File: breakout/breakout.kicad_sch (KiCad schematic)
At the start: 9 parts, among them J1 Glasgow, J2 ScrewTerminals, J3 SignalsMale, J4 SignalsFemale, J5 SignalsMale, J6 SignalsFemale, J7 TestPoints

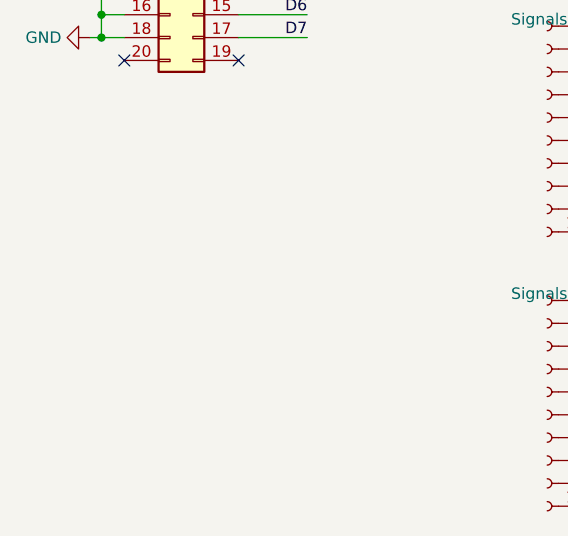
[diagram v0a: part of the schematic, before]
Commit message: [wip] add connector for generic fx2 logic analyzers
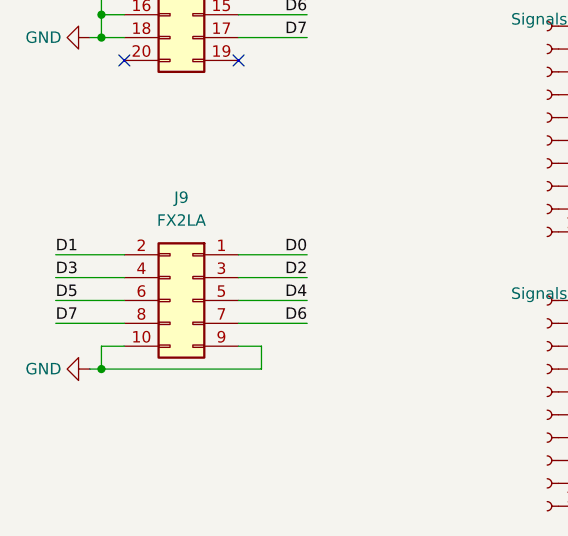
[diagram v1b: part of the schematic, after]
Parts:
- added J9: FX2LA, Connector_PinSocket_2.54mm:PinSocket_2x05_P2.54mm_Vertical, symbol Connector_Generic:Conn_02x05_Odd_Even
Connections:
- net D0: now also J9.1 (Pin_1)
- net D1: now also J9.2 (Pin_2)
- net D2: now also J9.3 (Pin_3)
- net D3: now also J9.4 (Pin_4)
- net D4: now also J9.5 (Pin_5)
- net D5: now also J9.6 (Pin_6)
- net D6: now also J9.7 (Pin_7)
- net D7: now also J9.8 (Pin_8)
- net GND: now also J9.10 (Pin_10), J9.9 (Pin_9)

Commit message: finished
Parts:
- J2: footprint TerminalBlock_Phoenix:TerminalBlock_Phoenix_MPT-0,5-12-2.54_1x12_P2.54mm_Horizontal -> Glasgow:TerminalBlock_not_WAGO_233-512_2x12_P2.54mm
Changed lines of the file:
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@@
 			)
 		)
-		(property "Footprint" "TerminalBlock_Phoenix:TerminalBlock_Phoenix_MPT-0,5-12-2.54_1x12_P2.54mm_Horizontal"
+		(property "Footprint" "Glasgow:TerminalBlock_not_WAGO_233-512_2x12_P2.54mm"
 			(at 171.45 81.28 0)
 			(effects

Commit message: wip? rev2
- rounded corners
- more LA space (todo confirm spacing re: glasgow center)
- vio/vsense connection switch
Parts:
- added SW1: SW_SPDT, Button_Switch_THT:SW_Slide_SPDT_Straight_CK_OS102011MS2Q, symbol Switch:SW_SPDT
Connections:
- net VBUS: now also SW1.2 (B)
- net VSENSE: now also SW1.3 (C)
- no-connect marks 2 -> 3
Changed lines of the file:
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@@
 	)
 	(no_connect
+		(at 73.66 34.29)
+	)
+	(no_connect
 		(at 77.47 92.71)
 	)
@@
 	(wire
 		(pts
+			(xy 55.88 34.29) (xy 55.88 36.83)
+		)
+		(stroke
+			(width 0)
+			(type default)
+		)
+	)
+	(wire
+		(pts
 			(xy 143.51 80.01) (xy 151.13 80.01)
 		)
@@
 	(wire
 		(pts
+			(xy 73.66 39.37) (xy 81.28 39.37)
+		)
+		(stroke
+			(width 0)
+			(type default)
+		)
+	)
+	(wire
+		(pts
 			(xy 143.51 72.39) (xy 151.13 72.39)
 		)
@@
 	(wire
 		(pts
+			(xy 55.88 36.83) (xy 63.5 36.83)
+		)
+		(stroke
+			(width 0)
+			(type default)
+		)
+	)
+	(wire
+		(pts
 			(xy 64.77 72.39) (xy 62.23 72.39)
 		)
@@
 		)
 	)
+	(label "VSENSE"
+		(at 81.28 39.37 180)
+		(fields_autoplaced yes)
+		(effects
+			(font
+				(size 1.27 1.27)
+			)
+			(justify right bottom)
+		)
+	)
 	(label "D1"
 		(at 124.46 124.46 180)
@@
 	)
 	(symbol
+		(lib_id "power:VBUS")
+		(at 55.88 34.29 0)
+		(mirror y)
+		(unit 1)
+		(exclude_from_sim no)
+		(in_bom yes)
+		(on_board yes)
+		(dnp no)
+		(fields_autoplaced yes)
+		(property "Reference" "#PWR014"
+			(at 55.88 38.1 0)
+			(effects
+				(font
+					(size 1.27 1.27)
+				)
+				(hide yes)
+			)
+		)
+		(property "Value" "VBUS"
+			(at 55.88 30.1569 0)
+			(effects
+				(font
+					(size 1.27 1.27)
+				)
+			)
+		)
+		(property "Footprint" ""
+			(at 55.88 34.29 0)
+			(effects
+				(font
+					(size 1.27 1.27)
+				)
+				(hide yes)
+			)
+		)
+		(property "Datasheet" ""
+			(at 55.88 34.29 0)
+			(effects
+				(font
+					(size 1.27 1.27)
+				)
+				(hide yes)
+			)
+		)
+		(property "Description" "Power symbol creates a global label with name \"VBUS\""
+			(at 55.88 34.29 0)
+			(effects
+				(font
+					(size 1.27 1.27)
+				)
+				(hide yes)
+			)
+		)
+		(pin "1"
+		)
+		(instances
+			(project "breakout"
+				(path "/611ff545-19b3-4976-9e7e-acfa9fe1d3fb"
+					(reference "#PWR014")
+					(unit 1)
+				)
+			)
+		)
+	)
+	(symbol
 		(lib_id "power:GND")
 		(at 120.65 142.24 90)
@@
 					(unit 1)
 				)
+			)
+		)
+	)
+	(symbol
+		(lib_id "Switch:SW_SPDT")
+		(at 68.58 36.83 0)
+		(unit 1)
+		(exclude_from_sim no)
+		(in_bom yes)
+		(on_board yes)
+		(dnp no)
+		(fields_autoplaced yes)
+		(property "Reference" "SW1"
+			(at 68.58 27.94 0)
+			(effects
+				(font
+					(size 1.27 1.27)
+				)
+			)
+		)
+		(property "Value" "SW_SPDT"
+			(at 68.58 30.48 0)
+			(effects
+				(font
+					(size 1.27 1.27)
+				)
+			)
+		)
+		(property "Footprint" "Button_Switch_THT:SW_Slide_SPDT_Straight_CK_OS102011MS2Q"
+			(at 68.58 36.83 0)
+			(effects
+				(font
+					(size 1.27 1.27)
+				)
+				(hide yes)
+			)
+		)
+		(property "Datasheet" "~"
+			(at 68.58 44.45 0)
+			(effects
+				(font
+					(size 1.27 1.27)
+				)
+				(hide yes)
+			)
+		)
+		(property "Description" "Switch, single pole double throw"
+			(at 68.58 36.83 0)
+			(effects
+				(font
+					(size 1.27 1.27)
+				)
+				(hide yes)
+			)
+		)
+		(pin "2"
+		)
+		(pin "1"
+		)
+		(pin "3"
+		)
+		(instances
+			(project ""
+				(path "/611ff545-19b3-4976-9e7e-acfa9fe1d3fb"
+					(reference "SW1")
+					(unit 1)
+				)
